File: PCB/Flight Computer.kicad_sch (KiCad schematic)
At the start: 0 parts

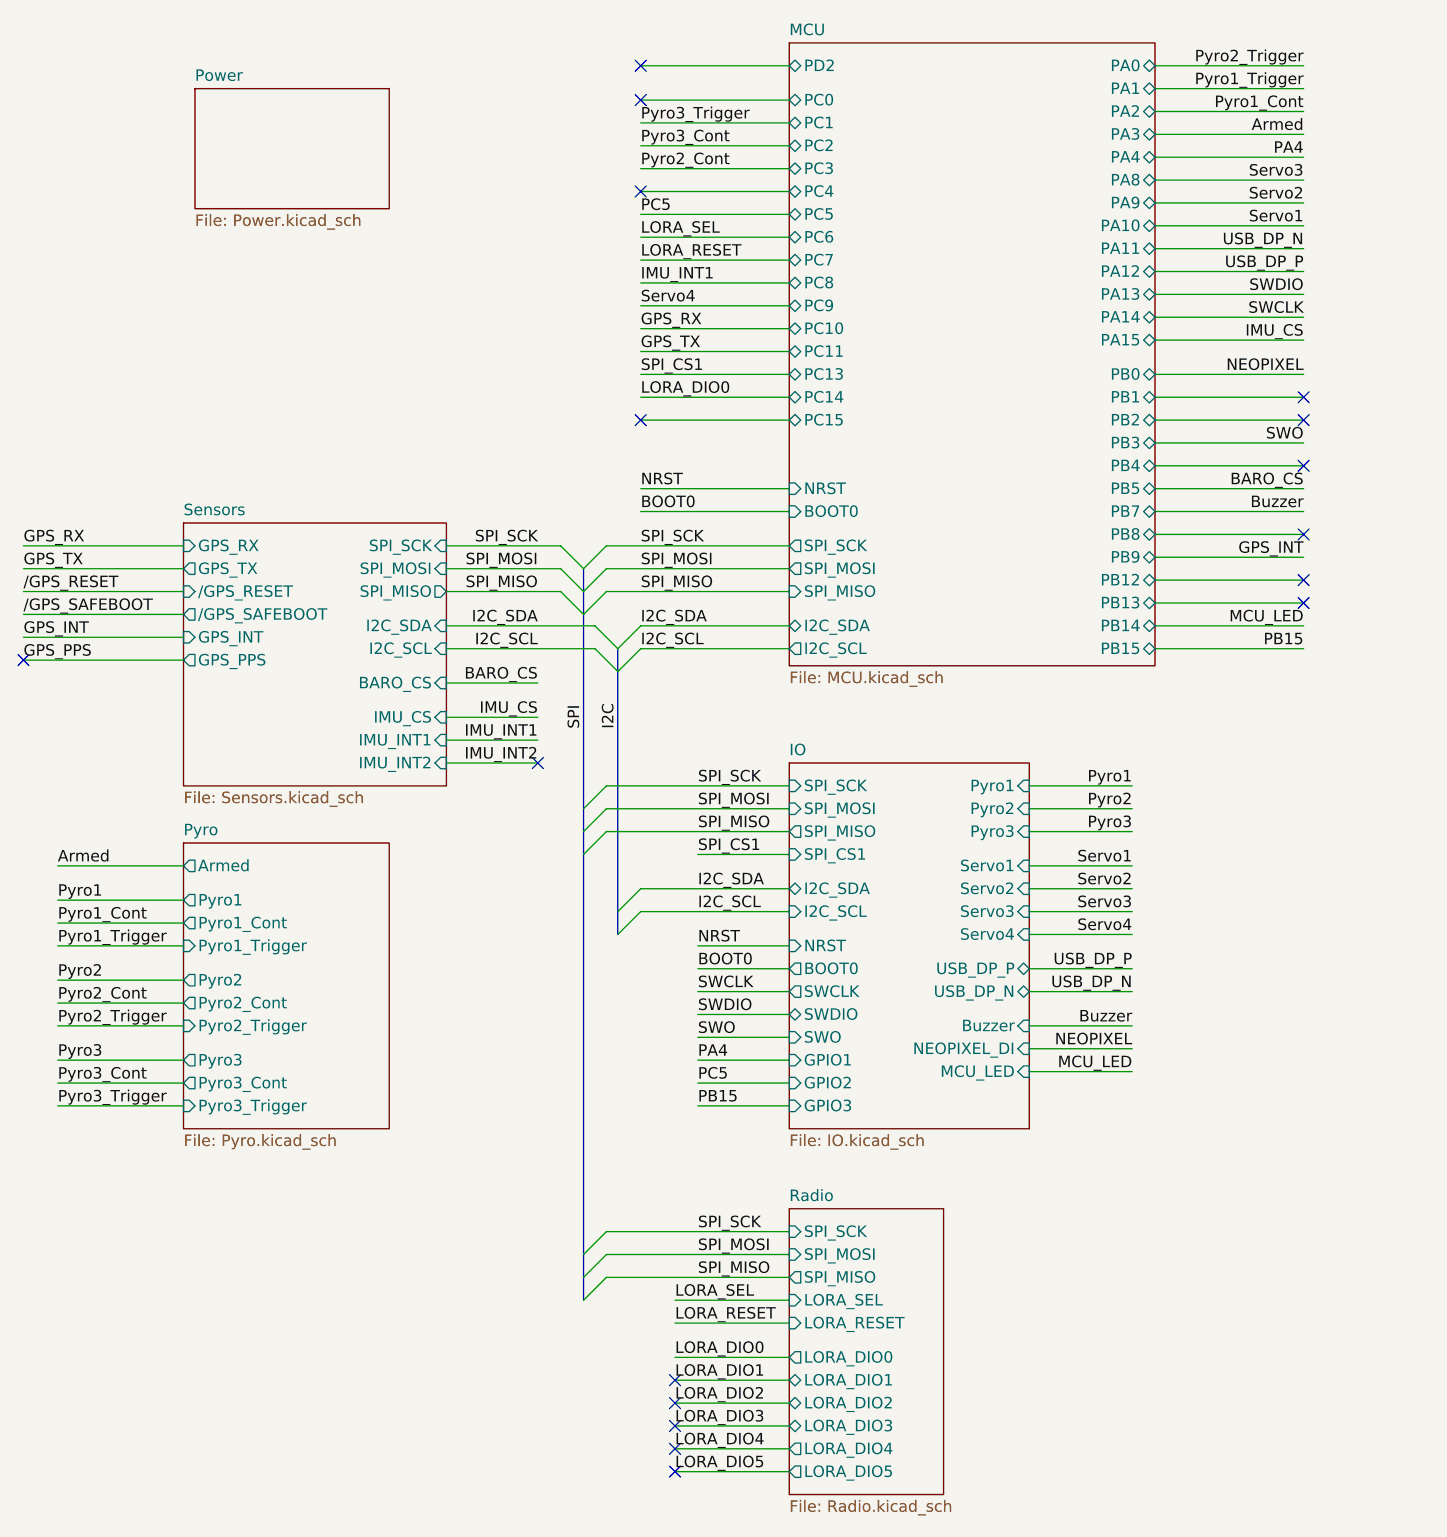
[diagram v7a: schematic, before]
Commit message: - Renamed all NETs connected to MCU sheet to the pin name - Cleaned up schematic - Named all unnamed NETs
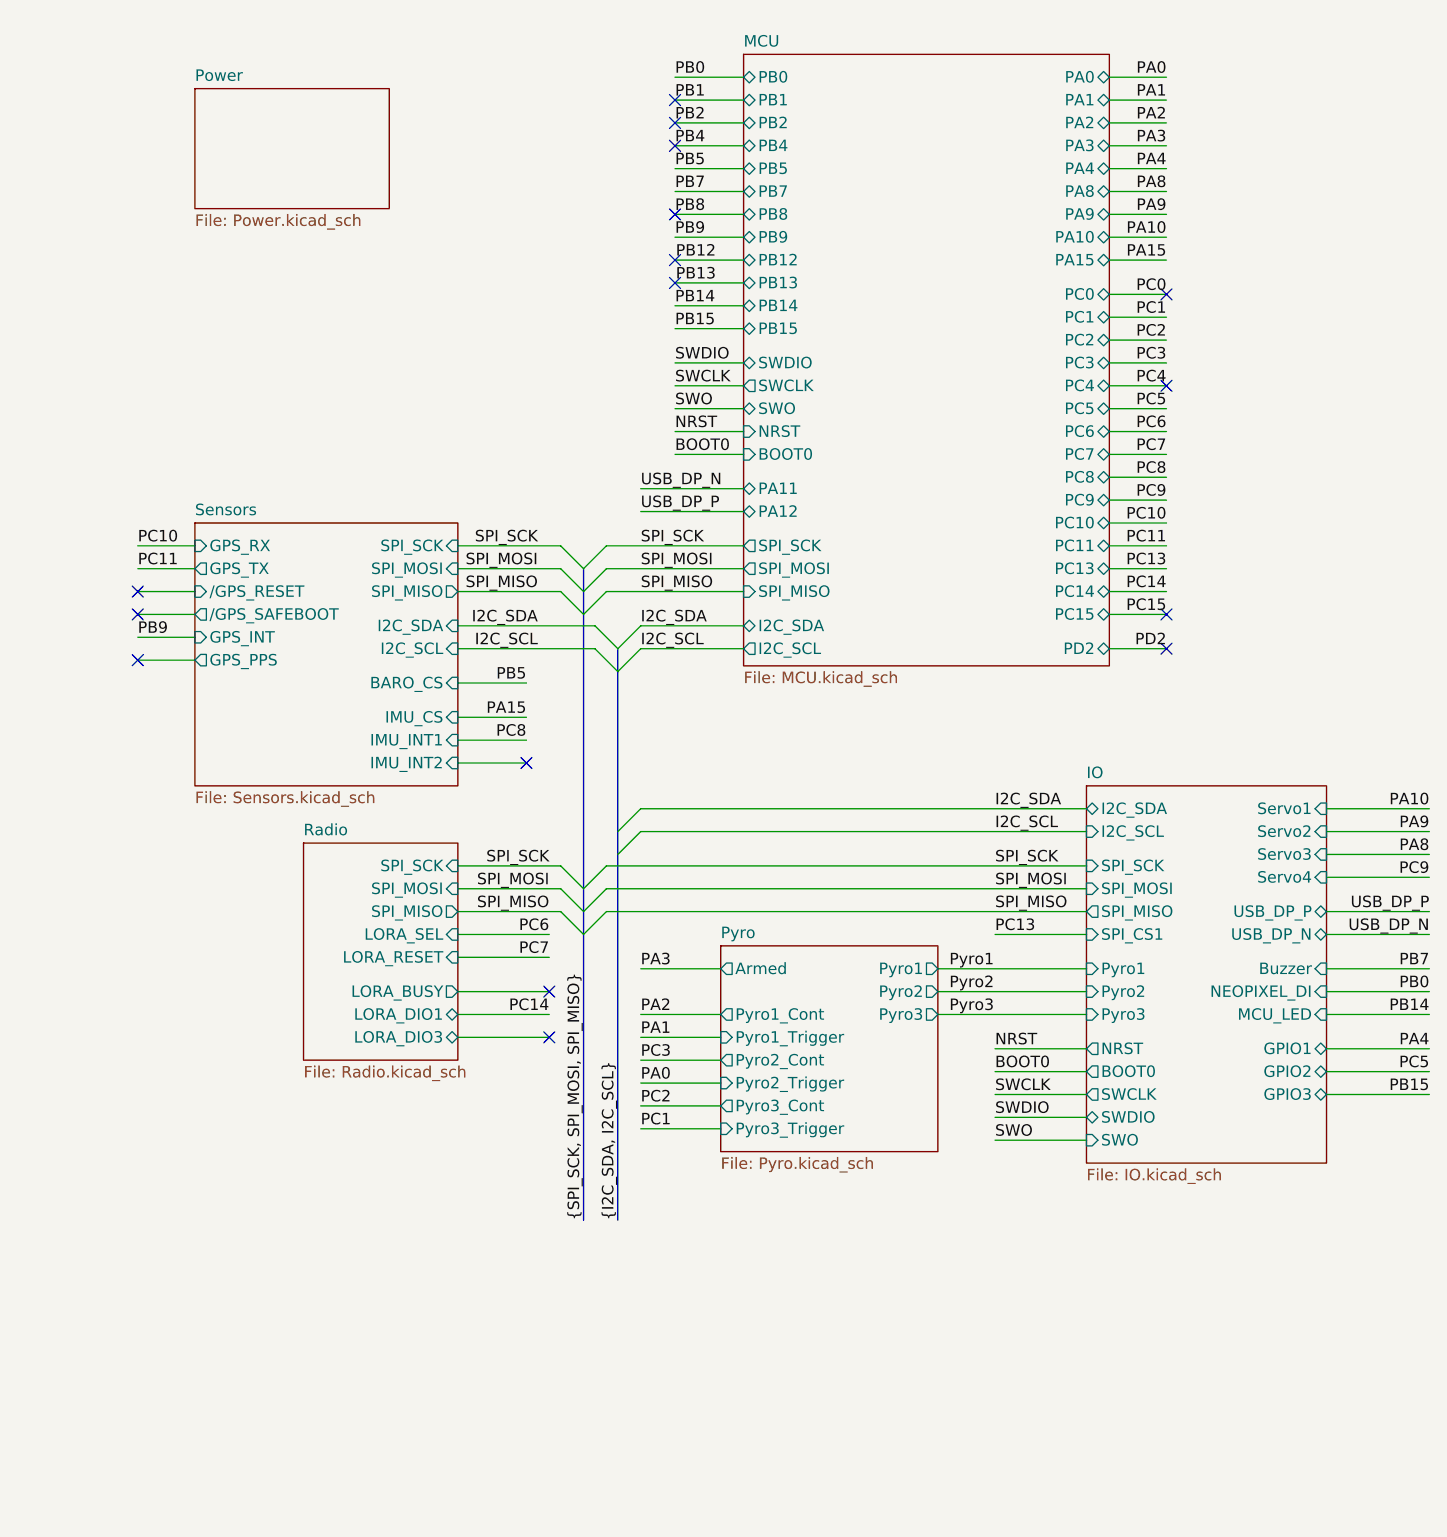
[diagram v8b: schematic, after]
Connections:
- no-connect marks 17 -> 16
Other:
- sheet MCU ports: added SWCLK, SWDIO, SWO; removed PA13, PA14, PB3
- sheet Radio ports: added LORA_BUSY; removed LORA_DIO0, LORA_DIO2, LORA_DIO4, LORA_DIO5
